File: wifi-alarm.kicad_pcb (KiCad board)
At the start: 2 copper layers, 101.1 x 100.2 mm, 119 parts, among them IC1 TPS563300DRLR, IC2 MMSZ5231BS-7-F, J1 Screw_Terminal_01x02, J2 DM3AT-SF-PEJM5_40_, J3 Conn_ARM_JTAG_SWD_20, J4 Screw_Terminal_01x14, J5 USB_C_Receptacle_USB2.0_14P, K1 Relay_SPDT, K2 Relay_SPDT, K3 Relay_SPDT, Q1 MMBT2222A, Q2 MMBT2222A, Q3 MMBT2222A, Q4 MMBT2222A, Q5 MMBT2222A, Q8 TIP41, Q9 TIP41, U1 AMS1117-3.3, U2 ESP32-S3-WROOM-1, U3 CP2104, U4 PC817, U5 PC817, U6 PC817

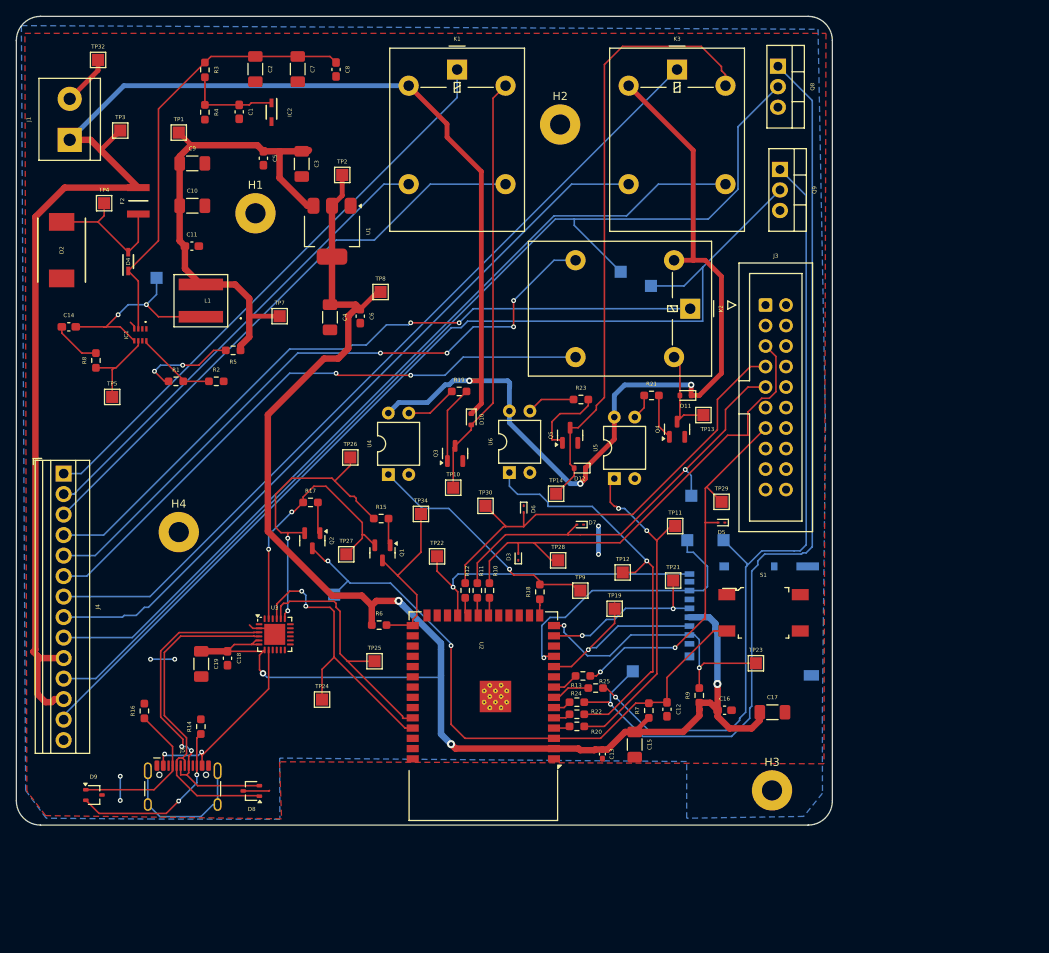
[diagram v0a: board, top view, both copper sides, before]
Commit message: Add w5500 LAN to SPI because S3 does not have RMII, so we can't use LAN8720
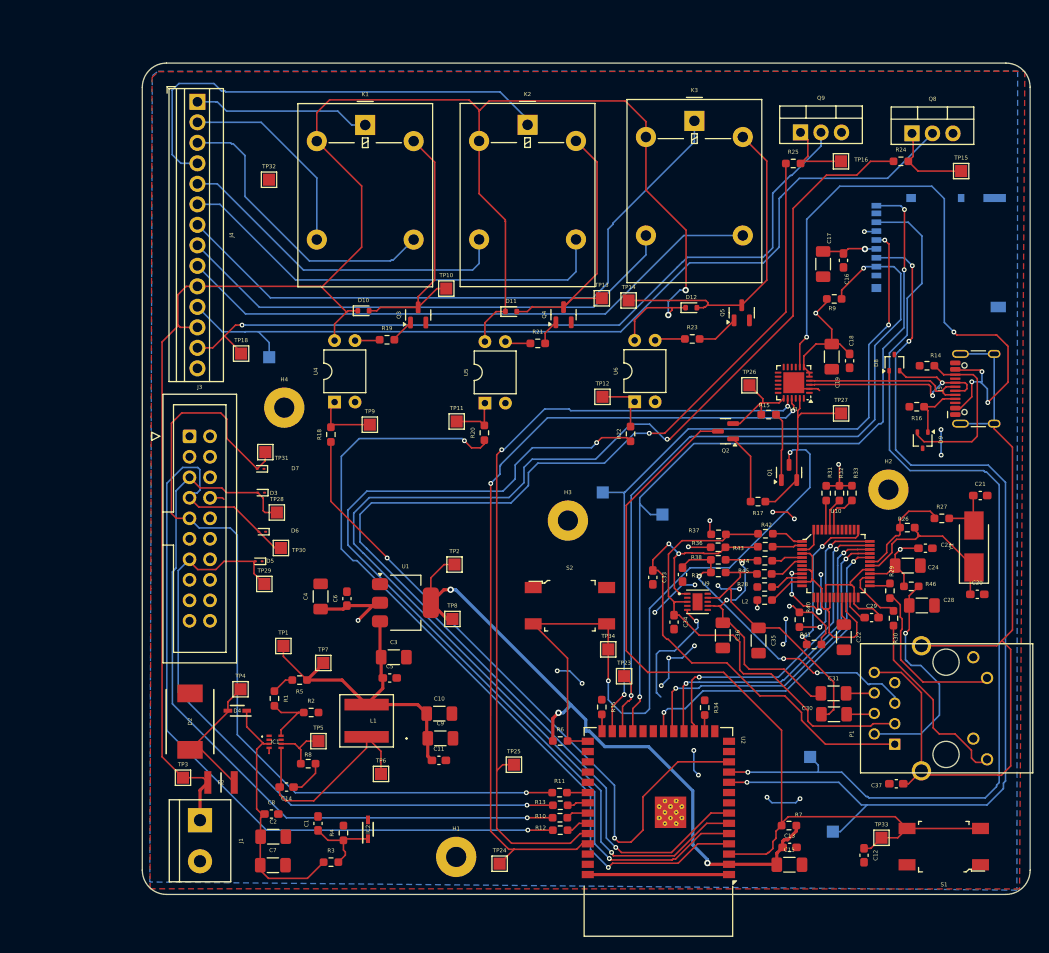
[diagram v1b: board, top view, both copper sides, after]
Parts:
- added C20: 18p, Capacitor_SMD:C_0603_1608Metric_Pad1.08x0.95mm_HandSolder, F.Cu at (168.9, 106.2)
- added C21: 18p, Capacitor_SMD:C_0603_1608Metric_Pad1.08x0.95mm_HandSolder, F.Cu at (169.3, 94.0)
- added C22: 4.7u, Capacitor_SMD:C_1206_3216Metric_Pad1.33x1.80mm_HandSolder, F.Cu at (152.4, 111.5)
- added C23: 100n, Capacitor_SMD:C_0603_1608Metric_Pad1.08x0.95mm_HandSolder, F.Cu at (162.5, 100.5)
- added C24: 22u, Capacitor_SMD:C_1206_3216Metric_Pad1.33x1.80mm_HandSolder, F.Cu at (160.3, 102.7)
- added C25: 10n, Capacitor_SMD:C_0603_1608Metric_Pad1.08x0.95mm_HandSolder, F.Cu at (132.4, 103.8)
- added C28: 22n, Capacitor_SMD:C_1206_3216Metric_Pad1.33x1.80mm_HandSolder, F.Cu at (162.1, 107.6)
- added C29: 10n, Capacitor_SMD:C_0603_1608Metric_Pad1.08x0.95mm_HandSolder, F.Cu at (155.8, 109.1)
- added C30: 6.8u, Capacitor_SMD:C_1206_3216Metric_Pad1.33x1.80mm_HandSolder, F.Cu at (151.2, 121.1)
- added C31: 6.8u, Capacitor_SMD:C_1206_3216Metric_Pad1.33x1.80mm_HandSolder, F.Cu at (151.1, 118.5)
- added C33: 18p, Capacitor_SMD:C_0603_1608Metric_Pad1.08x0.95mm_HandSolder, F.Cu at (128.7, 104.1)
- added C34: 18p, Capacitor_SMD:C_0603_1608Metric_Pad1.08x0.95mm_HandSolder, F.Cu at (131.4, 109.7)
- added C35: 10u, Capacitor_SMD:C_1206_3216Metric_Pad1.33x1.80mm_HandSolder, F.Cu at (141.8, 111.9)
- added C36: 10u, Capacitor_SMD:C_1206_3216Metric_Pad1.33x1.80mm_HandSolder, F.Cu at (137.4, 111.3)
- added C37: 1n 2kV, Capacitor_SMD:C_0603_1608Metric_Pad1.08x0.95mm_HandSolder, F.Cu at (158.9, 129.7)
- added L2: LCMGG160808T121RG, Resistor_SMD:R_0603_1608Metric_Pad0.98x0.95mm_HandSolder, F.Cu at (142.6, 106.9)
- added P1: J1B1211CCD, footprints:J1B1211CCD, F.Cu at (165.1, 120.3)
- added R26: 1M, Resistor_SMD:R_0603_1608Metric_Pad0.98x0.95mm_HandSolder, F.Cu at (160.3, 97.9)
- added R27: 0, Resistor_SMD:R_0603_1608Metric_Pad0.98x0.95mm_HandSolder, F.Cu at (164.5, 96.8)
- added R28: 12.4k 1%, Resistor_SMD:R_0603_1608Metric_Pad0.98x0.95mm_HandSolder, F.Cu at (142.6, 105.3)
- added R29: 330, Resistor_SMD:R_0603_1608Metric_Pad0.98x0.95mm_HandSolder, F.Cu at (158.1, 105.8)
- added R30: 330, Resistor_SMD:R_0603_1608Metric_Pad0.98x0.95mm_HandSolder, F.Cu at (158.6, 109.2)
- added R31: 10K, Resistor_SMD:R_0603_1608Metric_Pad0.98x0.95mm_HandSolder, F.Cu at (150.2, 93.7)
- added R32: 10K, Resistor_SMD:R_0603_1608Metric_Pad0.98x0.95mm_HandSolder, F.Cu at (151.8, 93.7)
- added R33: 10K, Resistor_SMD:R_0603_1608Metric_Pad0.98x0.95mm_HandSolder, F.Cu at (153.4, 93.7)
- added R34: 10k, Resistor_SMD:R_0603_1608Metric_Pad0.98x0.95mm_HandSolder, F.Cu at (135.2, 120.2)
- added R35: 10k, Resistor_SMD:R_0603_1608Metric_Pad0.98x0.95mm_HandSolder, F.Cu at (122.4, 120.2)
- added R36: 49.9, Resistor_SMD:R_0603_1608Metric_Pad0.98x0.95mm_HandSolder, F.Cu at (136.8, 100.4)
- added R37: 49.9, Resistor_SMD:R_0603_1608Metric_Pad0.98x0.95mm_HandSolder, F.Cu at (136.9, 98.8)
- added R38: 49.9, Resistor_SMD:R_0603_1608Metric_Pad0.98x0.95mm_HandSolder, F.Cu at (136.8, 101.9)
- added R39: 49.9, Resistor_SMD:R_0603_1608Metric_Pad0.98x0.95mm_HandSolder, F.Cu at (136.8, 103.5)
- added R40: 10K, Resistor_SMD:R_0603_1608Metric_Pad0.98x0.95mm_HandSolder, F.Cu at (146.9, 109.4)
- added R41: 10K, Resistor_SMD:R_0603_1608Metric_Pad0.98x0.95mm_HandSolder, F.Cu at (148.7, 112.4)
- added R42: 0, Resistor_SMD:R_0603_1608Metric_Pad0.98x0.95mm_HandSolder, F.Cu at (142.7, 98.7)
- added R43: 0, Resistor_SMD:R_0603_1608Metric_Pad0.98x0.95mm_HandSolder, F.Cu at (142.7, 100.3)
- added R44: 0, Resistor_SMD:R_0603_1608Metric_Pad0.98x0.95mm_HandSolder, F.Cu at (142.6, 102.0)
- added R45: 0, Resistor_SMD:R_0603_1608Metric_Pad0.98x0.95mm_HandSolder, F.Cu at (142.5, 103.7)
- added R46: 10, Resistor_SMD:R_0603_1608Metric_Pad0.98x0.95mm_HandSolder, F.Cu at (160.8, 105.2)
- added S2: FSM4JSMATR, digikey-footprints:Switch_Tactile_SMD_6x6mm, F.Cu at (118.5, 107.6)
- added U10: W5500, digikey-footprints:LQFP-48_7x7mm, F.Cu at (151.4, 102.4)
- added U9: ESD1014MUTAG, footprints:SON50P260X260X55-11N, F.Cu at (134.3, 107.1)
- added Y1: 25MHz Crystal, Crystal:Crystal_SMD_5032-2Pin_5.0x3.2mm_HandSoldering, F.Cu at (168.5, 100.3)
- C13: footprint Capacitor_SMD:C_0402_1005Metric_Pad0.74x0.62mm_HandSolder -> Capacitor_SMD:C_0603_1608Metric_Pad1.08x0.95mm_HandSolder
- TP15, TP16, TP18, TP31, TP33, TP6: moved to F.Cu
- TP19, TP21, TP22: moved to B.Cu
- moved D9 111.7 mm to (162.2, 87.1), turned to -90 degrees
- moved J5 111.5 mm to (169.9, 80.7), turned to 90 degrees
- moved R16 102.8 mm to (161.4, 83.0), turned to 180 degrees
- moved R14 100.5 mm to (162.7, 77.9), turned to 180 degrees
- moved R3 99.4 mm to (88.9, 139.4), turned to 0 degrees
- moved C7 98.7 mm to (81.7, 139.8), turned to 0 degrees
- moved D8 95.7 mm to (158.7, 77.5), turned to 90 degrees
- moved C2 95.1 mm to (81.7, 136.2), turned to 0 degrees
- moved C8 92.6 mm to (81.5, 133.4), turned to 0 degrees
- moved R4 90.9 mm to (90.4, 135.8), turned to 90 degrees
- moved IC2 89.6 mm to (93.4, 135.3), turned to 90 degrees
- moved C1 88.7 mm to (87.2, 134.6), turned to 90 degrees
- moved C19 86.9 mm to (150.9, 76.8)
- moved J1 85.8 mm to (72.6, 134.2), turned to -90 degrees
- moved C18 85.4 mm to (153.1, 77.3)
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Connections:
- R10 pad 2: Net-(U2-IO12) -> Net-(U2-IO41)
- R11 pad 2: Net-(U2-IO13) -> Net-(U2-IO39)
- R12 pad 2: Net-(U2-IO14) -> Net-(U2-IO42)
- R13 pad 2: Net-(U2-IO15) -> Net-(U2-IO40)
- S1 pad 1: unconnected-(S1-Pad1) -> GND
- S1 pad 4: unconnected-(S1-Pad4) -> /EN
- U2 pad 12: unconnected-(U2-IO8-Pad12) -> /RL_1
- U2 pad 13: /SD_CLK -> unconnected-(U2-IO19-Pad13)
- U2 pad 14: /SD_CS -> unconnected-(U2-IO20-Pad14)
- U2 pad 15: /RL_1 -> unconnected-(U2-IO3-Pad15)
- U2 pad 16: unconnected-(U2-IO46-Pad16) -> Net-(U2-IO46)
- U2 pad 17: unconnected-(U2-IO9-Pad17) -> /ETH_MOSI
- U2 pad 18: unconnected-(U2-IO10-Pad18) -> /ETH_MISO
- U2 pad 19: unconnected-(U2-IO11-Pad19) -> /ETH_SCLK
- U2 pad 20: Net-(U2-IO12) -> /ETH_SCS
- U2 pad 21: Net-(U2-IO13) -> unconnected-(U2-IO13-Pad21)
- U2 pad 22: Net-(U2-IO14) -> unconnected-(U2-IO14-Pad22)
- U2 pad 24: unconnected-(U2-IO47-Pad24) -> /SD_CS
- U2 pad 25: unconnected-(U2-IO48-Pad25) -> /SD_CLK
- U2 pad 26: unconnected-(U2-IO45-Pad26) -> Net-(U2-IO45)
- U2 pad 32: unconnected-(U2-IO39-Pad32) -> Net-(U2-IO39)
- U2 pad 33: unconnected-(U2-IO40-Pad33) -> Net-(U2-IO40)
- U2 pad 34: unconnected-(U2-IO41-Pad34) -> Net-(U2-IO41)
- U2 pad 35: unconnected-(U2-IO42-Pad35) -> Net-(U2-IO42)
- U2 pad 8: Net-(U2-IO15) -> unconnected-(U2-IO15-Pad8)
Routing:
- net /TR_1: track 2.20 -> 167.2 mm, vias 0 -> 2
- net /TR_2: track 4.73 -> 153.2 mm, vias 0 -> 2
- net /RL_3: track 2.11 -> 112.8 mm, vias 0 -> 2
- net Net-(Q8-B): track 117.1 -> 10.8 mm, vias 1 -> 0
- net /RL_2: track 2.01 -> 101.2 mm, vias 0 -> 2
- net /SD_MOSI: track 26.0 -> 123.6 mm, vias 1 -> 3
- net Net-(Q9-B): track 99.9 -> 9.71 mm, vias 1 -> 0
- net /SD_MISO: track 35.2 -> 124.8 mm
- net Earth: track 18.2 -> 102.8 mm
- net /RL_1: track 2.02 -> 84.6 mm, vias 0 -> 2
- net GND: track 23.7 -> 94.6 mm, vias 6 -> 22
- net /Tx: track 31.2 -> 101.0 mm, vias 0 -> 2
- net /SD_CLK: track 21.7 -> 91.4 mm, vias 2 -> 3
- net /IO0: track 22.1 -> 90.5 mm, vias 0 -> 2
- net /w5500/TXP: track 0.00 -> 66.5 mm, vias 0 -> 2
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- added copper zone on B.Cu, net /3.3V_OUT
- removed copper zone on B.Cu, net GND
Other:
- board size 101.1 x 100.2 mm -> 110 x 103 mm
- board text removed: "BOTSGEEK WIFI ALARM V 0.1"
